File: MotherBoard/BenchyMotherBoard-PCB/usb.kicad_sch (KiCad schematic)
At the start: 92 parts, among them J10 USB3_B, J11 USB3-PORT2, J12 USB3-PORT3, J13 USB3-PORT4, J14 USB3-PORT5, J15 USB-INTERNAL-PORT1, J16 TFT-DISPLAY, J17 USB-INTERNAL-PORT2, J9 USB3-PORT1, Q3 RQ5A030AP, U1 STM32MP157FAB1, U10 USB7206C, U12 UCS2114, U13 UCS2114, U14 UCS2114, U15 LM317L, U16 AS321, U17 24LC08, U18 USB2412, Y3 25MHz, Y4 25MHz

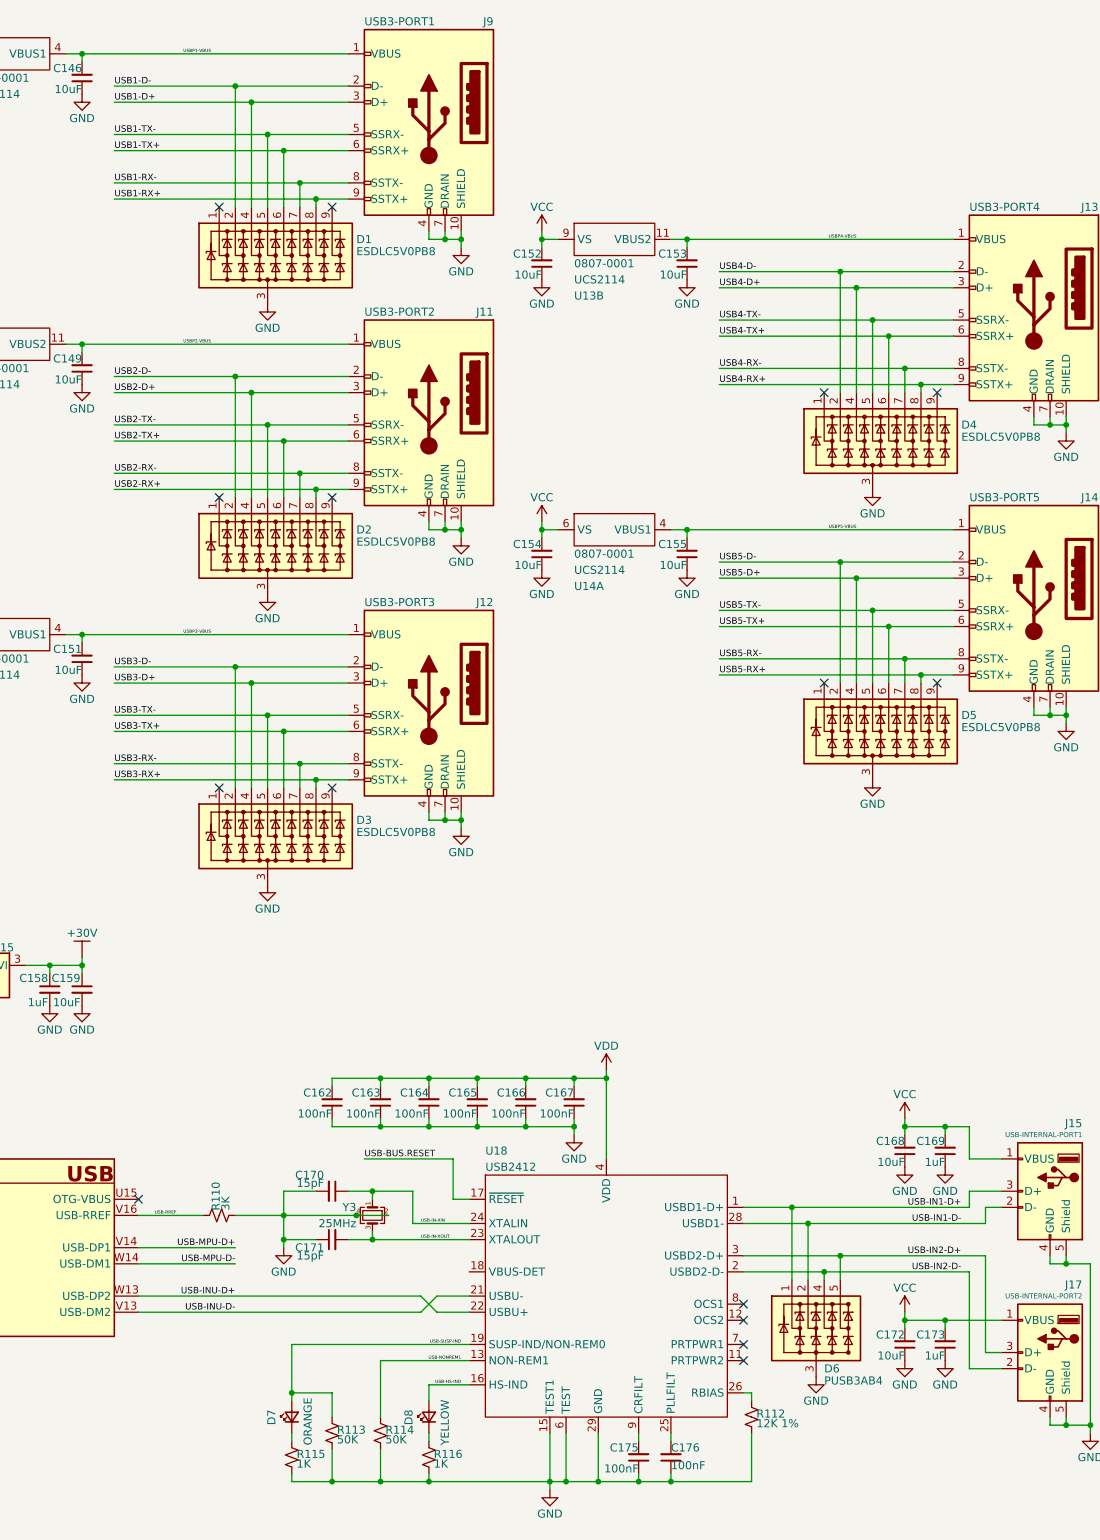
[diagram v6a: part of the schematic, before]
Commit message: Mostly routed USB
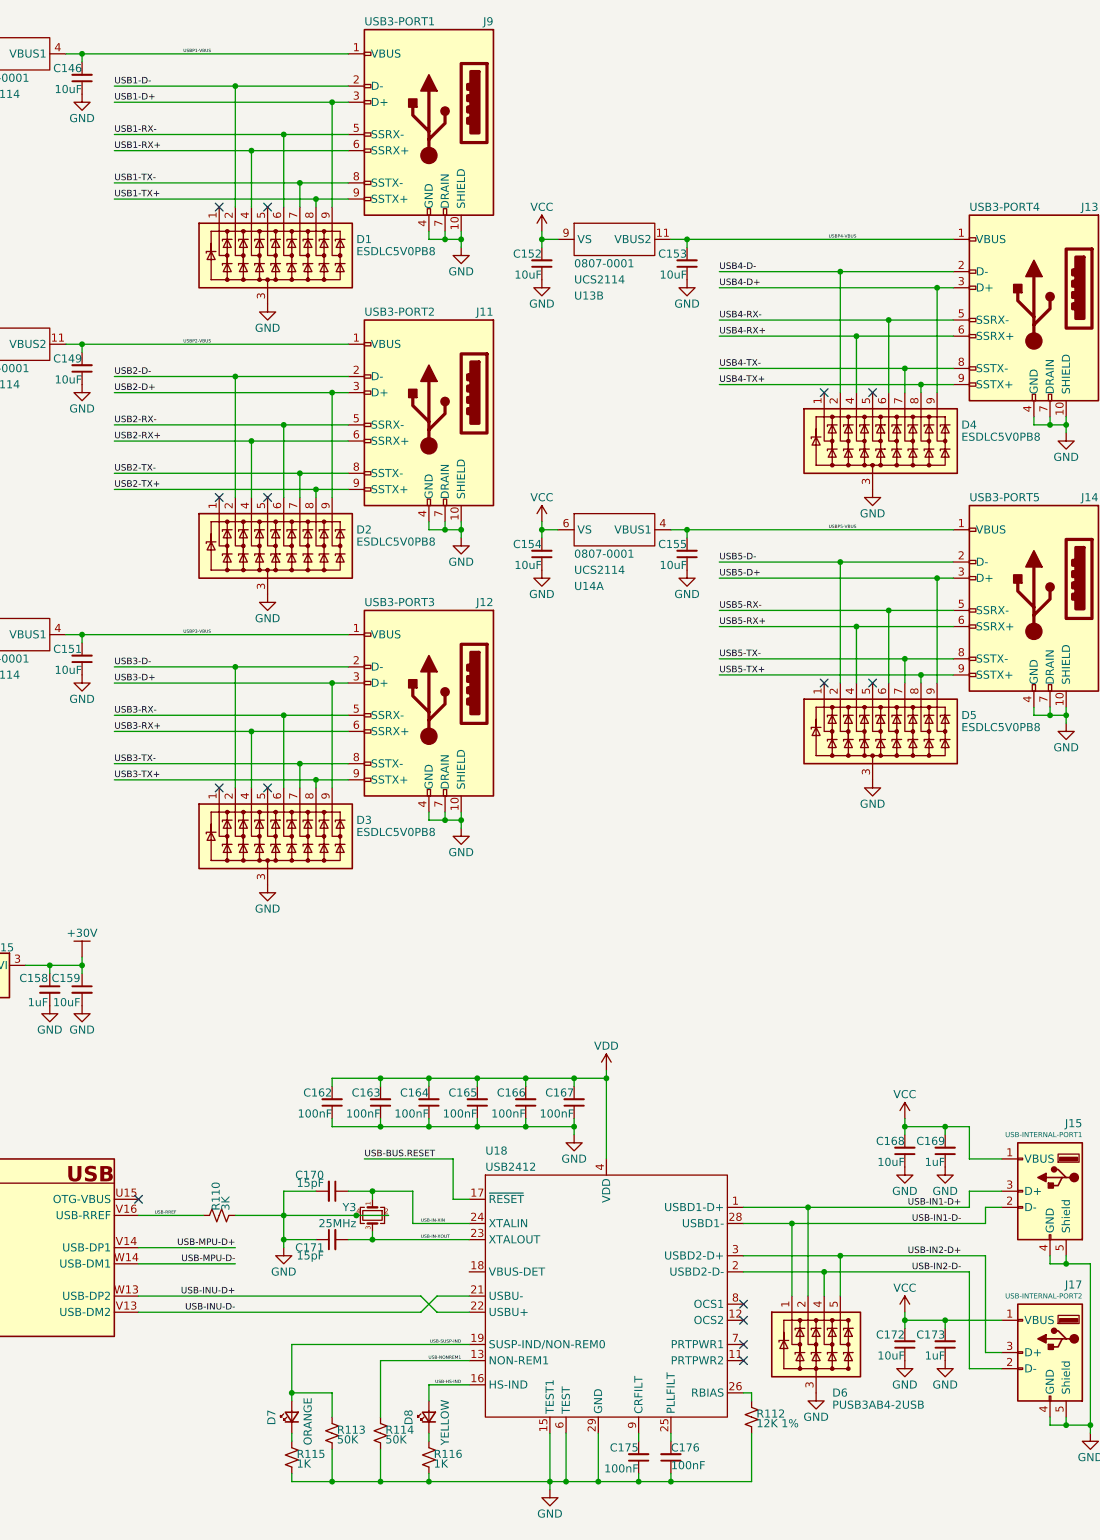
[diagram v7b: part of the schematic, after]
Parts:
- removed D6: PUSB3AB4, Daxxn_Packages:DFN2510A-10, symbol Daxxn_Protection:PUSB3AB4
- added D6: PUSB3AB4-2USB, Daxxn_Packages:DFN2510A-10, symbol Daxxn_Protection:PUSB3AB4-2USB
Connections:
- net GND: now also D6.3 (A), D6.8 (A)
- net USB-IN1-D+: now also D6.2 (K2), D6.9 (NC)
- net USB-IN1-D-: now also D6.1 (K1), D6.10 (NC)
- net USB-IN2-D+: now also D6.5 (K4), D6.6 (NC)
- net USB-IN2-D-: now also D6.4 (K3), D6.7 (NC)
- net USB1-D+: now also D1.9 (K8); no longer D1.4 (K3)
- net USB1-RX+: now also D1.4 (K3), J9.6 (SSRX+); no longer D1.8 (K7), J9.9 (SSTX+)
- net USB1-RX-: now also D1.6 (K5), J9.5 (SSRX-); no longer D1.7 (K6), J9.8 (SSTX-)
- net USB1-TX+: now also D1.8 (K7), J9.9 (SSTX+); no longer D1.6 (K5), J9.6 (SSRX+)
- net USB1-TX-: now also D1.7 (K6), J9.8 (SSTX-); no longer D1.5 (K4), J9.5 (SSRX-)
- net USB2-D+: now also D2.9 (K8); no longer D2.4 (K3)
- net USB2-RX+: now also D2.4 (K3), J11.6 (SSRX+); no longer D2.8 (K7), J11.9 (SSTX+)
- net USB2-RX-: now also D2.6 (K5), J11.5 (SSRX-); no longer D2.7 (K6), J11.8 (SSTX-)
- net USB2-TX+: now also D2.8 (K7), J11.9 (SSTX+); no longer D2.6 (K5), J11.6 (SSRX+)
- net USB2-TX-: now also D2.7 (K6), J11.8 (SSTX-); no longer D2.5 (K4), J11.5 (SSRX-)
- net USB3-D+: now also D3.9 (K8); no longer D3.4 (K3)
- net USB3-RX+: now also D3.4 (K3), J12.6 (SSRX+); no longer D3.8 (K7), J12.9 (SSTX+)
- net USB3-RX-: now also D3.6 (K5), J12.5 (SSRX-); no longer D3.7 (K6), J12.8 (SSTX-)
- net USB3-TX+: now also D3.8 (K7), J12.9 (SSTX+); no longer D3.6 (K5), J12.6 (SSRX+)
- net USB3-TX-: now also D3.7 (K6), J12.8 (SSTX-); no longer D3.5 (K4), J12.5 (SSRX-)
- net USB4-D+: now also D4.9 (K8); no longer D4.4 (K3)
- net USB4-RX+: now also D4.4 (K3), J13.6 (SSRX+); no longer D4.8 (K7), J13.9 (SSTX+)
- net USB4-RX-: now also D4.6 (K5), J13.5 (SSRX-); no longer D4.7 (K6), J13.8 (SSTX-)
- net USB4-TX+: now also D4.8 (K7), J13.9 (SSTX+); no longer D4.6 (K5), J13.6 (SSRX+)
- net USB4-TX-: now also D4.7 (K6), J13.8 (SSTX-); no longer D4.5 (K4), J13.5 (SSRX-)
- net USB5-D+: now also D5.9 (K8); no longer D5.4 (K3)
- net USB5-RX+: now also D5.4 (K3), J14.6 (SSRX+); no longer D5.8 (K7), J14.9 (SSTX+)
- net USB5-RX-: now also D5.6 (K5), J14.5 (SSRX-); no longer D5.7 (K6), J14.8 (SSTX-)
- net USB5-TX+: now also D5.8 (K7), J14.9 (SSTX+); no longer D5.6 (K5), J14.6 (SSRX+)
- net USB5-TX-: now also D5.7 (K6), J14.8 (SSTX-); no longer D5.5 (K4), J14.5 (SSRX-)

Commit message: Most routing completed
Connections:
- net USB-BUS.BRIGHT is gone; now on net DISP-BUS.BRIGHT: R103.1
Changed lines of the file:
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@@
     (effects (font (size 0.5 0.5)) (justify right bottom))
   )
-  (label "USB-BUS.BRIGHT" (at 184.15 185.42 0) (fields_autoplaced)
+  (label "DISP-BUS.BRIGHT" (at 184.15 185.42 0) (fields_autoplaced)
     (effects (font (size 1.016 1.016)) (justify left bottom))
   )
